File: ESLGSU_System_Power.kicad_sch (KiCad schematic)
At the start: 53 parts, among them Q1 DMN67D7L-7, U2 DMT3006LDK-7, U26 AP63203WU-7, U27 AP63205WU-7, U28 TPS2121RUXR, U3 INA219AIDCNR, U4 DML3012LDC-7, U5 AP74700QW6-7, U6 DMT3006LDK-7, U7 DML3012LDC-7, U8 AP74700QW6-7

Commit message: Schematic work
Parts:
- removed U7: DML3012LDC-7, Package_DFN_QFN:WDFN-12-1EP_3x3mm_P0.45mm_EP1.7x2.5mm, symbol ESLGSU_Parts_Lib:DML3012LDC-7
- added U7: NCP45770IMN24TWG, Package_DFN_QFN:WDFN-12-1EP_3x3mm_P0.45mm_EP1.7x2.5mm, symbol ESLGSU_Parts_Lib:NCP45770
- C10, C12, C3, C5, C7, C85, C89, C93: LCSC Part (none) -> C307331
- C11, C6: LCSC Part (none) -> C1523
- C2, C8: LCSC Part (none) -> C52923
- C20: LCSC Part (none) -> C45783
- C20: LCSC Part (none) -> C15850
- C4, C9: LCSC Part (none) -> C1532
- D1: LCSC Part (none) -> C2286
- L5, L6: value IHLP2020CZER4R7M11 -> SPM5020T-4R7M-LR; LCSC Part (none) -> C307807
- Q1: value DMN67D7L-7 -> RE1C002UNTCL; footprint Package_TO_SOT_SMD:SOT-23 -> Package_TO_SOT_SMD:SOT-416; LCSC Part (none) -> C509959
- R1, R4: LCSC Part (none) -> C25744
- R2, R5: value 100R -> 20K; LCSC Part (none) -> C25765
- R3: LCSC Part (none) -> C346483
- R8: value 150R -> 200R; LCSC Part (none) -> C25087
- R82: value 25.5K -> 27K; LCSC Part (none) -> C25771
- R83, R85: LCSC Part (none) -> C25741
- R84, R86: LCSC Part (none) -> C25908
- TP1: JLCPCB BOM (none) -> 0; now left out of the parts list
- TP1: footprint TestPoint:TestPoint_Pad_D2.0mm -> TestPoint:TestPoint_Pad_D1.5mm; JLCPCB BOM (none) -> 0; now left out of the parts list
- U2, U6: value DMT3006LDK-7 -> VBQF1303; LCSC Part (none) -> C481054
- U26: LCSC Part (none) -> C780769
- U27: LCSC Part (none) -> C2071056
- U28: LCSC Part (none) -> C485916
- U3: LCSC Part (none) -> C87469
- U4: value DML3012LDC-7 -> NCP45770IMN24TWG; symbol ESLGSU_Parts_Lib:DML3012LDC-7 -> ESLGSU_Parts_Lib:NCP45770; LCSC Part (none) -> C892480
- U5, U8: LCSC Part (none) -> C5381661
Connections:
- net EN_BAT_UNREG: now also U7.11 (EN)
- net EN_P_IN_UNREG: now also U4.11 (EN); no longer U4.2 (EN)
- net GNDA: now also R2.2, R5.2, U4.6 (GND), U7.6 (GND); no longer U4.4 (GND)
- net POWER_IN: now also U4.12 (VIN); no longer U4.1 (VIN)
- net SYS_5V: now also U4.10 (VCC), U7.10 (VCC); no longer U4.3 (VCC)
- net VBAT: now also U7.12 (VIN), U7.13 (VIN)
- net at C9.1, U6.2 (S), U8.6 (ANODE): now also U7.1 (VOUT), U7.2 (VOUT), U7.3 (VOUT), U7.4 (VOUT), U7.5 (VOUT); no longer R5.2
- net at Q1.1 (G), R4.2, U8.3 (EN): now also U7.8 (PG)
- net at R5.1: now also U7.9 (OCP)
- net at Q1.1 (G), R1.2, U5.3 (EN): now also U4.8 (PG); no longer U4.6 (PG)
- net at R2.1: now also U4.9 (OCP); no longer U4.7 (BLEED)
- net at C11.1: now also U7.7 (SR)
- net at U4.5 (VOUT): now also C4.1, U2.2 (S), U4.1 (VOUT), U4.2 (VOUT), U4.3 (VOUT), U4.4 (VOUT), U5.6 (ANODE); no longer C6.1
- new net: C6.1, U4.7 (SR)
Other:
- moved on the sheet: R2

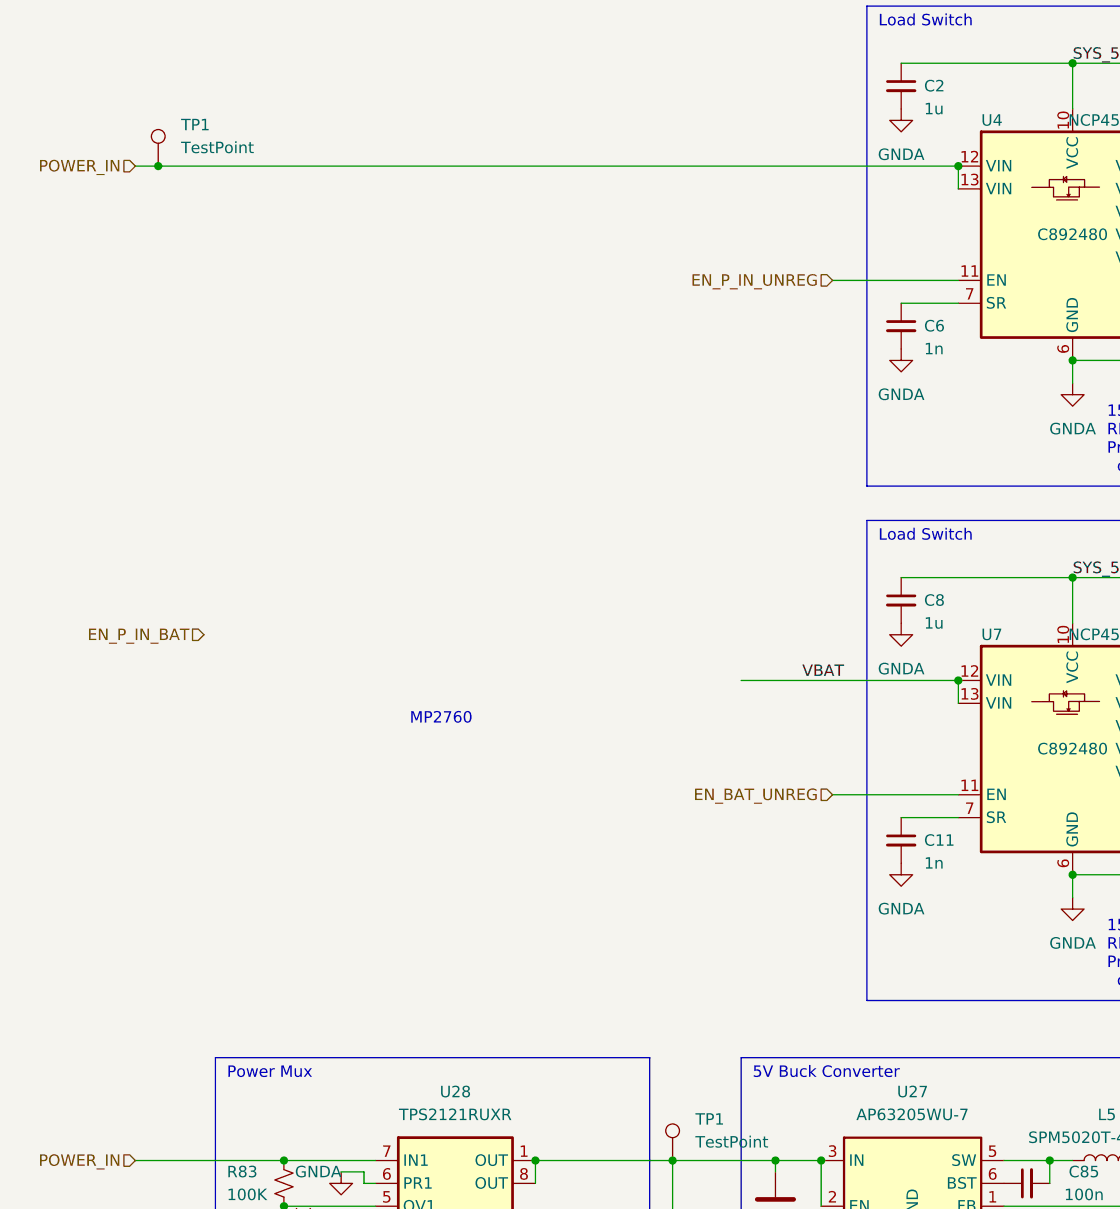
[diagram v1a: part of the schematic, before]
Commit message: Final schematic work, added battery charger, linked everything up
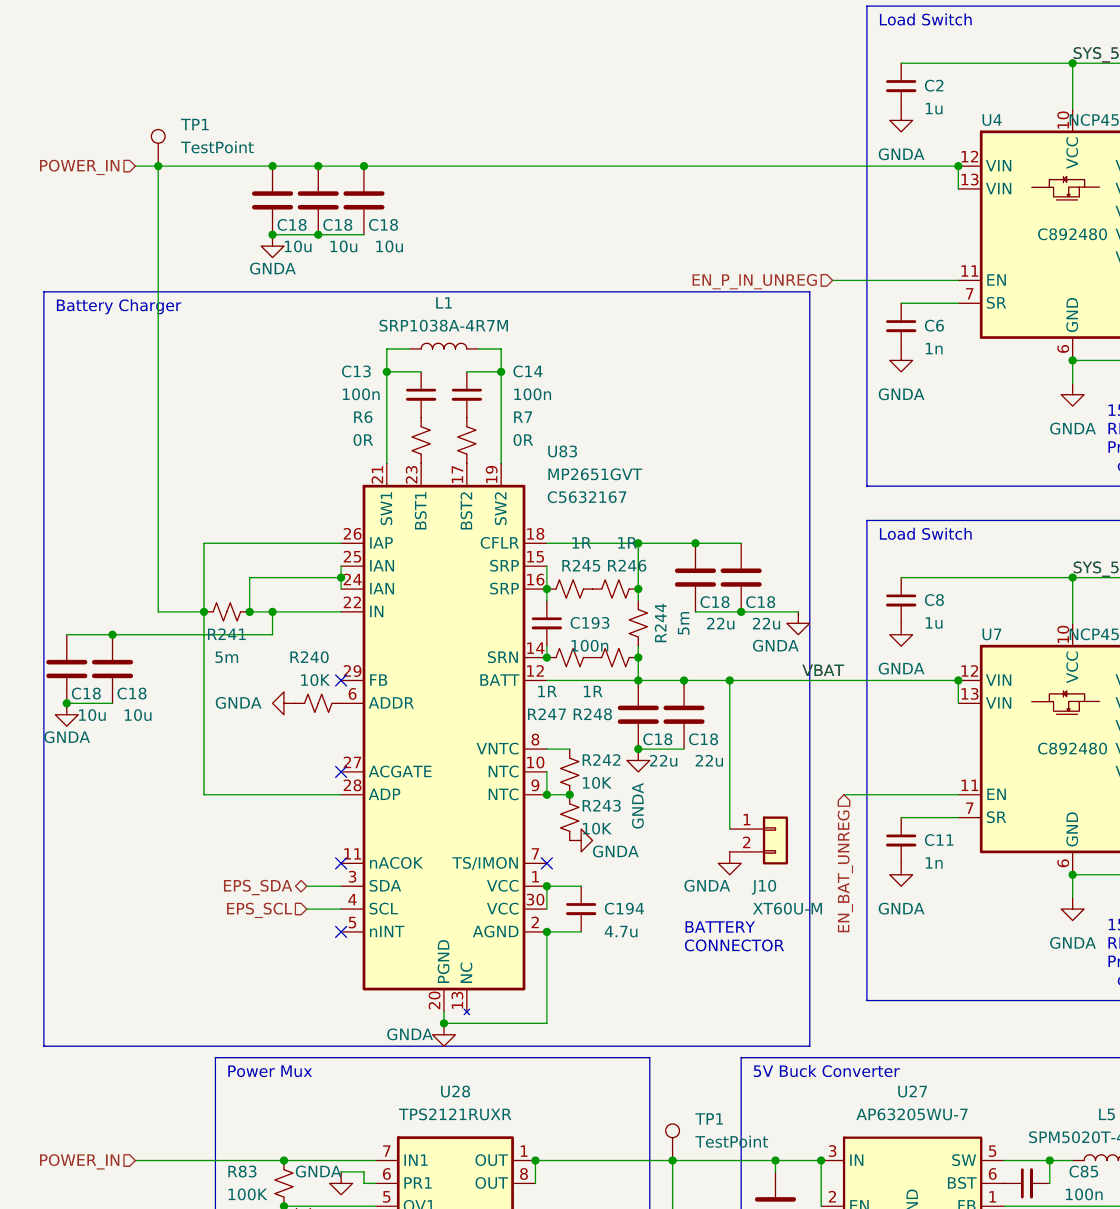
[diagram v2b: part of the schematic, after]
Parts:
- added C13, C14, C193: 100n, Capacitor_SMD:C_0402_1005Metric, symbol Device:C_Small
- added C18 (x5): 10u, Capacitor_SMD:C_0805_2012Metric, symbol Device:C
- added C18 (x4): 22u, Capacitor_SMD:C_0805_2012Metric, symbol Device:C
- added C194: 4.7u, Capacitor_SMD:C_0402_1005Metric, symbol Device:C_Small
- added J10: XT60U-M, symbol Connector_Generic:Conn_01x02
- added L1: SRP1038A-4R7M, Inductor_SMD:L_Vishay_IHLP-4040, symbol Device:L
- added R240, R242, R243: 10K, Resistor_SMD:R_0402_1005Metric, symbol Device:R_Small_US
- added R241, R244: 5m, Resistor_SMD:R_0603_1608Metric, symbol Device:R_Small_US
- added R245, R246, R247, R248: 1R, Resistor_SMD:R_0402_1005Metric, symbol Device:R_Small_US
- added R6, R7: 0R, Resistor_SMD:R_0402_1005Metric, symbol Device:R_Small_US
- added U83: MP2651GVT, symbol ESLGSU_Parts_Lib:MP2651GVT
- Q1: footprint Package_TO_SOT_SMD:SOT-416 -> Package_TO_SOT_SMD:SOT-23
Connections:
- net EPS_SCL: now also U83.4 (SCL)
- net EPS_SDA: now also U83.3 (SDA)
- net GNDA: now also C18.2, C18.2, C18.2, C18.2, C18.2, C18.2, C18.2, C18.2, C18.2, C194.2, J10.2 (Pin_2), R240.1, R243.2, U83.2 (AGND), U83.20 (PGND)
- net POWER_IN: now also C18.1, C18.1, C18.1, R241.1, U83.26 (IAP), U83.28 (ADP)
- net VBAT: now also C18.1, C18.1, J10.1 (Pin_1), R244.1, R248.1, U83.12 (BATT)
- new net: R242.1, U83.8 (VNTC)
- new net: R242.2, R243.1, U83.10 (NTC), U83.9 (NTC)
- new net: C193.1, R245.2, U83.15 (SRP), U83.16 (SRP)
- new net: C193.2, R247.2, U83.14 (SRN)
- new net: C194.1, U83.1 (VCC), U83.30 (VCC)
- new net: C13.1, L1.1, U83.21 (SW1)
- new net: C13.2, R6.1
- new net: C14.1, L1.2, U83.19 (SW2)
- new net: C18.1, C18.1, R241.2, U83.22 (IN), U83.24 (IAN), U83.25 (IAN)
- new net: R6.2, U83.23 (BST1)
- new net: R247.1, R248.2
- new net: R245.1, R246.2
- new net: C18.1, C18.1, R244.2, R246.1, U83.18 (CFLR)
- new net: C14.2, R7.1
- new net: R240.2, U83.6 (ADDR)
- new net: R7.2, U83.17 (BST2)
- no-connect marks 0 -> 5
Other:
- note added: "BATTERY CONNECTOR"
- note added: "Battery Charger"
- note removed: "MP2760"

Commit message: Last tweaks on schematic
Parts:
- removed R241, R244: 5m, Resistor_SMD:R_0603_1608Metric, symbol Device:R_Small_US
- added C35: 100u, Capacitor_SMD:CP_Elec_6.3x7.7, symbol Device:C
- added R10, R9: 5m, Resistor_SMD:R_1206_3216Metric, symbol Device:R_Small_US
- added TP1 (x3): TestPoint, TestPoint:TestPoint_Pad_D1.5mm, symbol Connector:TestPoint
- J2: renamed from J10; footprint (none) -> ESLGSU_Parts_Lib:XT60; JLCPCB BOM (none) -> 0; now not fitted; now left out of the parts list
- R4: renamed from R3; footprint Resistor_SMD:R_0603_1608Metric -> Resistor_SMD:R_1206_3216Metric; LCSC Part C346483 -> C464975
- U7: renamed from U83; footprint (none) -> ESLGSU_Parts_Lib:TQFN30_MP2651
- renumbered C6 to C10, C7 to C11, C8 to C16, C193 to C17, C9 to C20, C10 to C21, C11 to C24, C12 to C25, C194 to C26, C85 to C27, C93 to C31, C89 to C32, L5 to L2, L6 to L3, R247 to R11, R248 to R12, R240 to R14, R4 to R15, R242 to R16, R243 to R17, R5 to R18, R83 to R19, R1 to R2, R84 to R20, R85 to R21, R86 to R22, R82 to R23, R2 to R3, R245 to R7, R246 to R8, U27 to U10, U28 to U11, U26 to U12, U7 to U8, U8 to U9
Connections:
- net GNDA: now also C35.2
- net POWER_IN: now also C35.1, R9.1
- net VBAT: now also R10.1, TP1.1
- net at C20.1, U6.2 (S), U8.1 (VOUT)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: now also TP1.1
- net at C18.1, C18.1, U7.22 (IN)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: now also R9.2
- net at C4.1, U2.2 (S), U4.1 (VOUT)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: now also TP1.1
- net at C18.1, C18.1, R8.1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: now also R10.2
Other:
- note added: "20A max, 24V max RDSon ~3.6mOhm Prot: UVLO, short, current, thermal"
- note added: "BATTERY CONNECTOR XT60"
- note removed: "15A max, 20V max RDSon 4.8-6.1mOhm Prot: UVLO, short, current, thermal"
- note removed: "BATTERY CONNECTOR"

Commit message: Finished initial revision of PCB
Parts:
- removed R12, R8: 1R, Resistor_SMD:R_0402_1005Metric, symbol Device:R_Small_US
- added C231, C232: 1u, Capacitor_SMD:C_0402_1005Metric, symbol Device:C_Small
- added C233: 100n, Capacitor_SMD:C_0402_1005Metric, symbol Device:C_Small
- added R276, R278: 1R, Resistor_SMD:R_0402_1005Metric, symbol Device:R_Small_US
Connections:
- net GNDA: now also C231.2, C232.2
- net POWER_IN: now also R278.1; no longer U7.26 (IAP)
- net VBAT: now also R11.1
- net at C18.1, C18.1, R10.2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: now also R7.1, C232.1
- net at C18.1, C18.1, R9.2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: now also C231.1, R276.1; no longer U7.24 (IAN), U7.25 (IAN)
- new net: C233.1, R276.2, U7.24 (IAN), U7.25 (IAN)
- new net: C233.2, R278.2, U7.26 (IAP)

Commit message: Finished for production
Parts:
- C18: LCSC Part C109040 -> C15850
- J2: JLCPCB BOM 0 -> (none)
- Q1: footprint Package_TO_SOT_SMD:SOT-23 -> Package_TO_SOT_SMD:SOT-416
- U11: footprint Package_DFN_QFN:Texas_VQFN-HR-12_2x2.5mm_P0.5mm_ThermalVias -> Package_DFN_QFN:Texas_VQFN-HR-12_2x2.5mm_P0.5mm
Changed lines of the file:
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@@
       (effects (font (size 1.27 1.27)) hide)
     )
-    (property "LCSC Part" "C109040" (at 51.2614 43.4113 0)
+    (property "LCSC Part" "C15850" (at 51.2614 43.4113 0)
       (effects (font (size 1.27 1.27)) hide)
     )
@@
       (effects (font (size 1.27 1.27)) (justify left))
     )
-    (property "Footprint" "Package_TO_SOT_SMD:SOT-23" (at 160.02 108.585 0)
+    (property "Footprint" "Package_TO_SOT_SMD:SOT-416" (at 160.02 108.585 0)
       (effects (font (size 1.27 1.27) italic) (justify left) hide)
     )
@@
       (effects (font (size 1.27 1.27)))
     )
-    (property "Footprint" "Package_DFN_QFN:Texas_VQFN-HR-12_2x2.5mm_P0.5mm_ThermalVias" (at 57.15 151.13 0)
+    (property "Footprint" "Package_DFN_QFN:Texas_VQFN-HR-12_2x2.5mm_P0.5mm" (at 57.15 151.13 0)
       (effects (font (size 1.27 1.27)) hide)
     )
@@
       (effects (font (size 1.27 1.27)) hide)
     )
-    (property "LCSC Part" "C109040" (at 23.3214 95.4813 0)
+    (property "LCSC Part" "C15850" (at 23.3214 95.4813 0)
       (effects (font (size 1.27 1.27)) hide)
     )
@@
       (effects (font (size 1.27 1.27)) hide)
     )
-    (property "LCSC Part" "C109040" (at 46.1814 43.4113 0)
+    (property "LCSC Part" "C15850" (at 46.1814 43.4113 0)
       (effects (font (size 1.27 1.27)) hide)
     )
@@
       (effects (font (size 1.27 1.27)) (justify left))
     )
-    (property "Footprint" "Package_TO_SOT_SMD:SOT-23" (at 160.02 51.435 0)
+    (property "Footprint" "Package_TO_SOT_SMD:SOT-416" (at 160.02 51.435 0)
       (effects (font (size 1.27 1.27) italic) (justify left) hide)
     )
@@
       (effects (font (size 1.27 1.27)) hide)
     )
-    (property "JLCPCB BOM" "0" (at 96.52 107.95 0)
-      (effects (font (size 1.27 1.27)) hide)
-    )
     (pin "1")
     (pin "2")
@@
       (effects (font (size 1.27 1.27)) hide)
     )
-    (property "LCSC Part" "C109040" (at 41.1014 43.4113 0)
+    (property "LCSC Part" "C15850" (at 41.1014 43.4113 0)
       (effects (font (size 1.27 1.27)) hide)
     )
@@
       (effects (font (size 1.27 1.27)) hide)
     )
-    (property "LCSC Part" "C109040" (at 18.2414 95.4813 0)
+    (property "LCSC Part" "C15850" (at 18.2414 95.4813 0)
       (effects (font (size 1.27 1.27)) hide)
     )

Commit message: Should be done with minimal version
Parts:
- C13, C14, C16, C17, C18, C20, C21, C231, C232, C233, C24, C25, C26, D1, L1, Q1, R10, R11, R14, R15, R16, R17, R18, R276, R278, R6, R7, R8, R9, U6, U7, U8, U9: now not fitted; now left out of the parts list

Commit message: Final V1 board with notes
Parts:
- U4, U8: footprint Package_DFN_QFN:WDFN-12-1EP_3x3mm_P0.45mm_EP1.7x2.5mm -> Package_DFN_QFN:DFN-12-1EP_3x3mm_P0.5mm_EP1.6x2.5mm
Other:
- note added: "Change address!!"
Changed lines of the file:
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@@
     (fill (type none))
+  )
+  (text "Change address!!" (at 248.92 43.18 0)
+    (effects (font (size 1.27 1.27)) (justify left bottom))
   )
   (text "BATTERY\nCONNECTOR\nXT60" (at 86.36 124.46 0)
@@
       (effects (font (size 1.27 1.27)))
     )
-    (property "Footprint" "Package_DFN_QFN:WDFN-12-1EP_3x3mm_P0.45mm_EP1.7x2.5mm" (at 118.11 86.36 0)
+    (property "Footprint" "Package_DFN_QFN:DFN-12-1EP_3x3mm_P0.5mm_EP1.6x2.5mm" (at 118.11 86.36 0)
       (effects (font (size 1.27 1.27)) hide)
     )
@@
       (effects (font (size 1.27 1.27)))
     )
-    (property "Footprint" "Package_DFN_QFN:WDFN-12-1EP_3x3mm_P0.45mm_EP1.7x2.5mm" (at 118.11 29.21 0)
-      (effects (font (size 1.27 1.27)) hide)
-    )
+    (property "Footprint" "Package_DFN_QFN:DFN-12-1EP_3x3mm_P0.5mm_EP1.6x2.5mm" (at 118.11 29.21 0)
+      (effects (font (size 1.27 1.27)) hide)
+    )
